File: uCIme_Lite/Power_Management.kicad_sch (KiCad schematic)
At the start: 13 parts

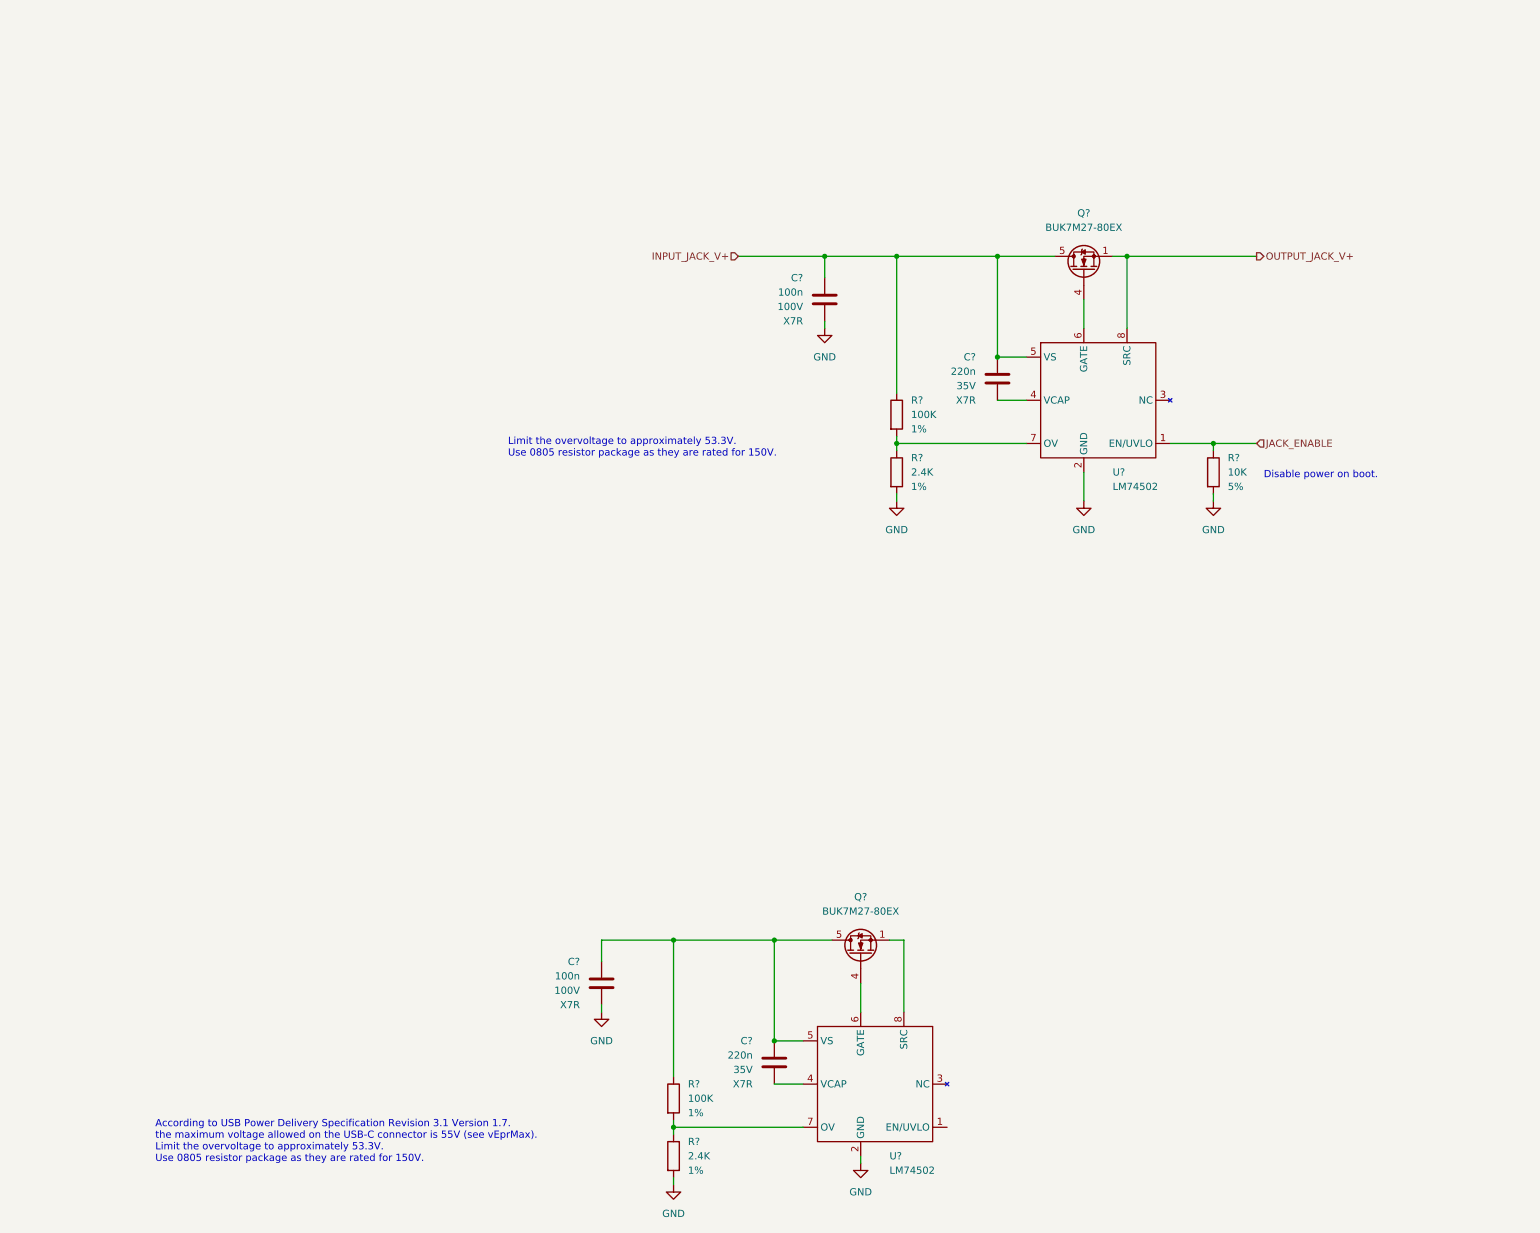
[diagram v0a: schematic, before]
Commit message: lite: Added USB-C connectors power control and data passthrough.
Signed-off-by: Adrien Ricciardi <aricciardi@baylibre.com>
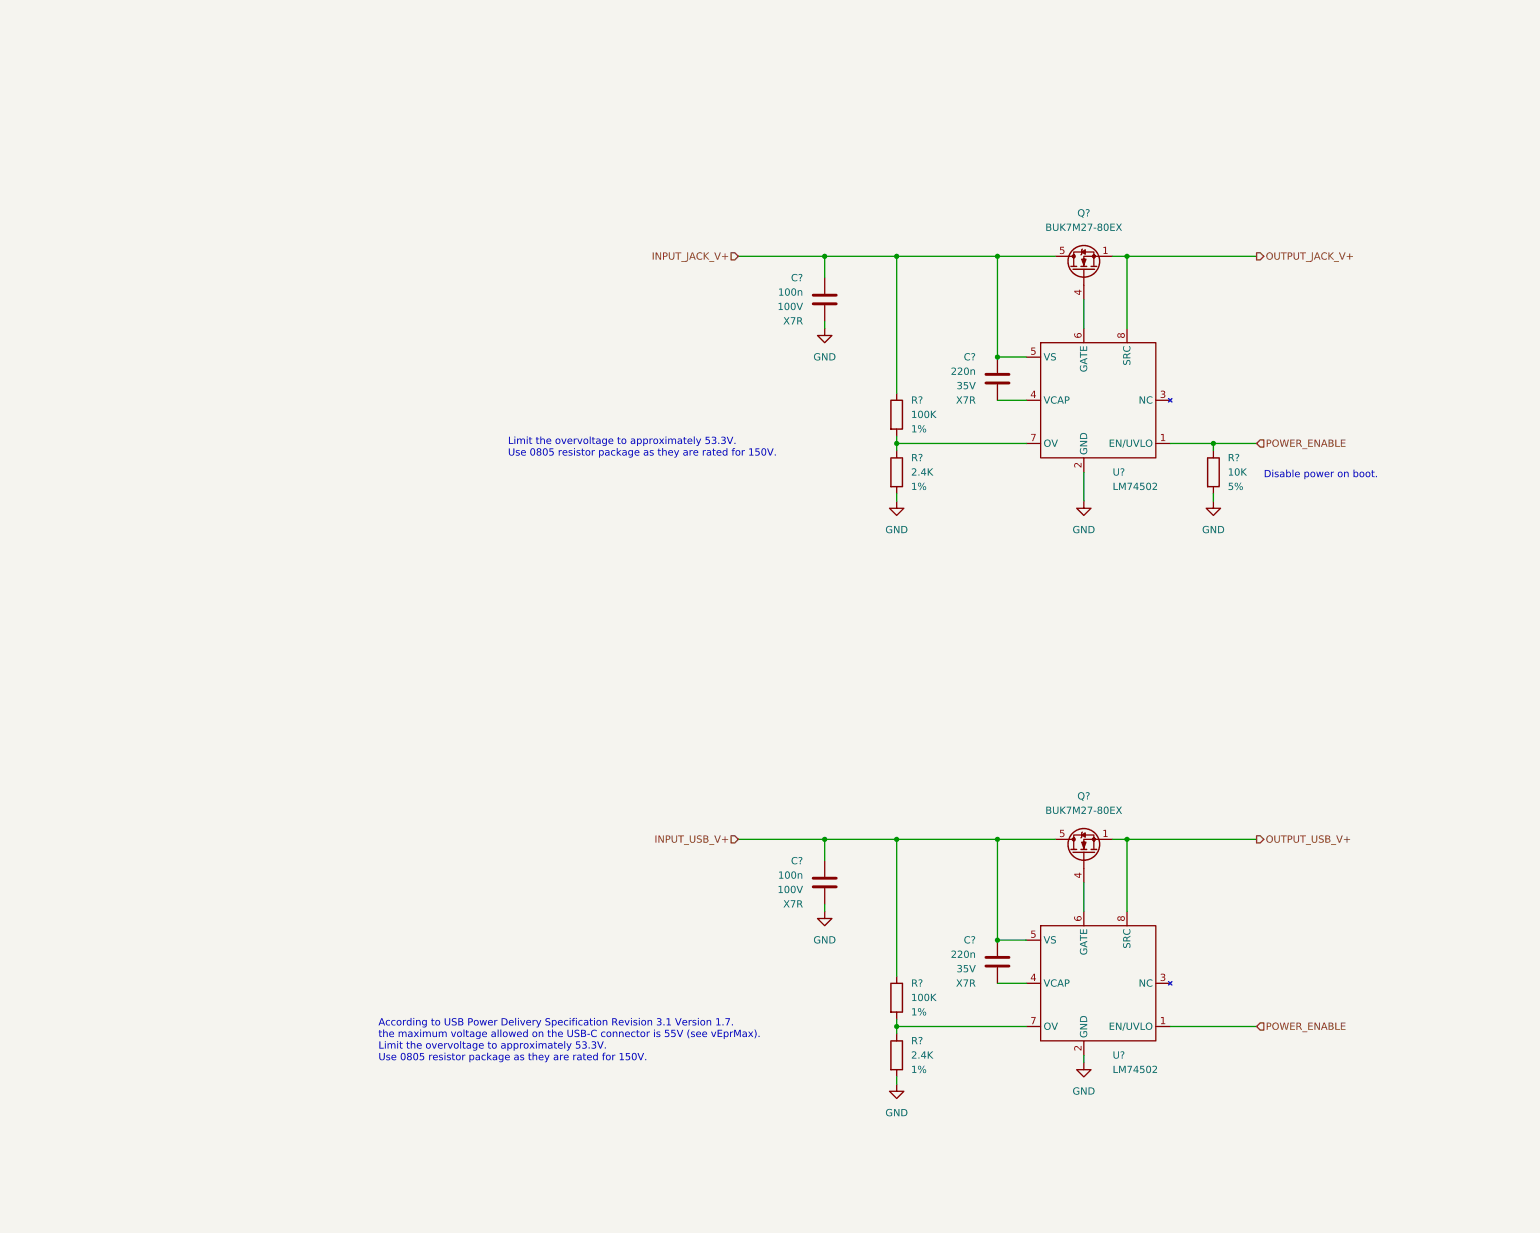
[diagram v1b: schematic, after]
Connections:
- net JACK_ENABLE is gone; now on net POWER_ENABLE: R?.1, U?.1 (EN/UVLO)
- net INPUT_USB_V+: now reaches C?.1, C?.1, Q?.5 (D), R?.1, U?.5 (VS)
- net OUTPUT_USB_V+: now reaches Q?.1 (S), Q?.2 (S), Q?.3 (S), U?.8 (SRC)
- net POWER_ENABLE: now reaches U?.1 (EN/UVLO)
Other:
- moved on the sheet: C?, Q?, R?, U?

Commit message: lite: Added FTDI USB connector, power supplies and USB differential pair to schematic.
Signed-off-by: Adrien Ricciardi <aricciardi@baylibre.com>
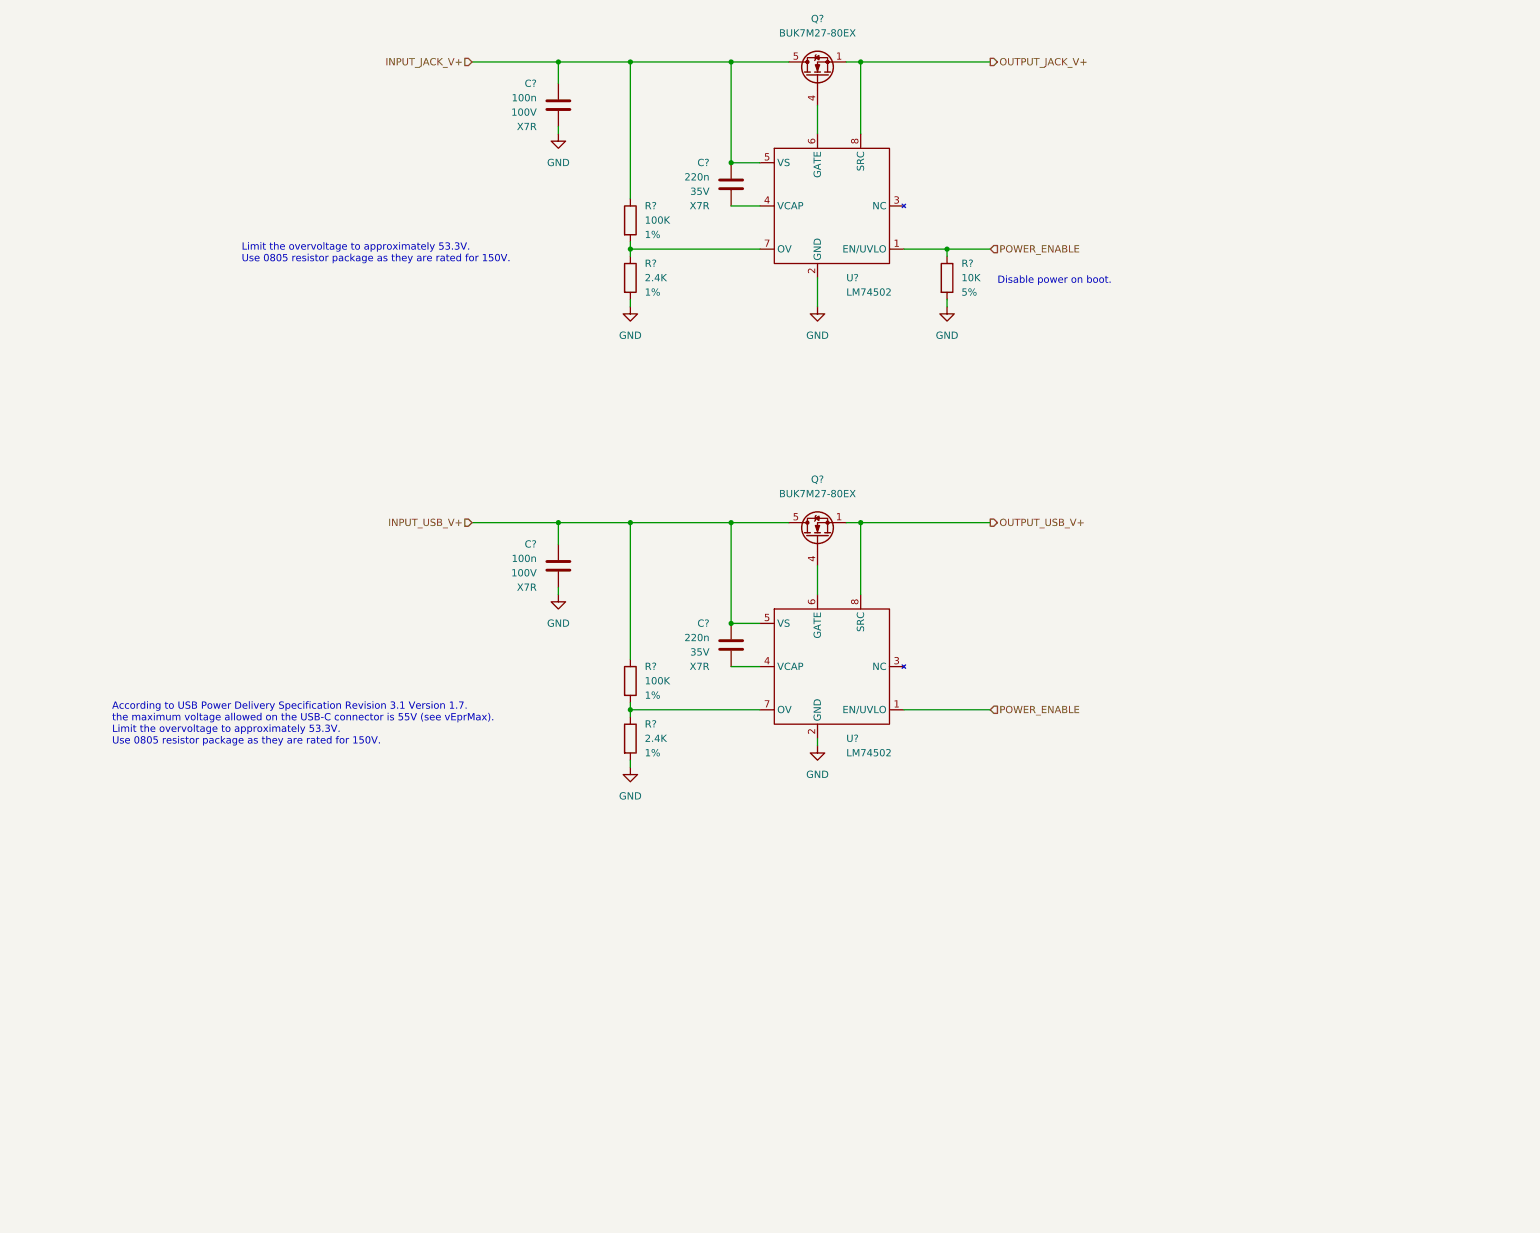
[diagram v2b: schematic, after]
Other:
- moved on the sheet: C?, Q?, R?, U?

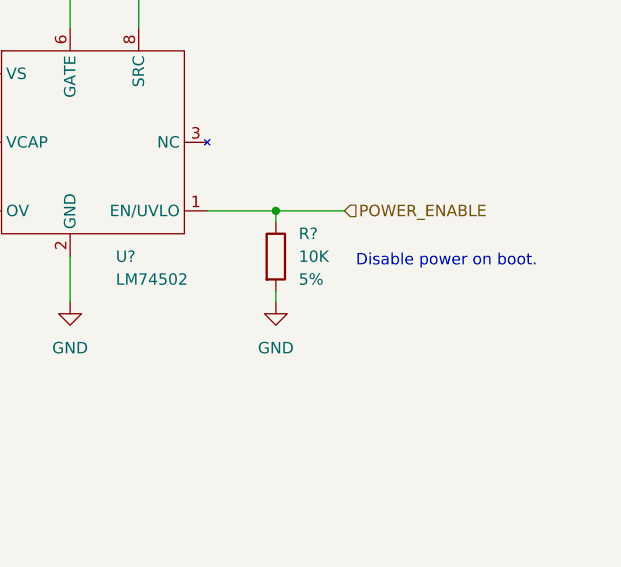
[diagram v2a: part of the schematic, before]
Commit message: lite: Added serial and USB connectors. A voltage translator is provided on the serial ports for the user to select the appropriate board voltage. No voltage translator is provided on the FTDI GPIO pins because they are meant to be used with custom extension boards.
Signed-off-by: Adrien Ricciardi <aricciardi@baylibre.com>
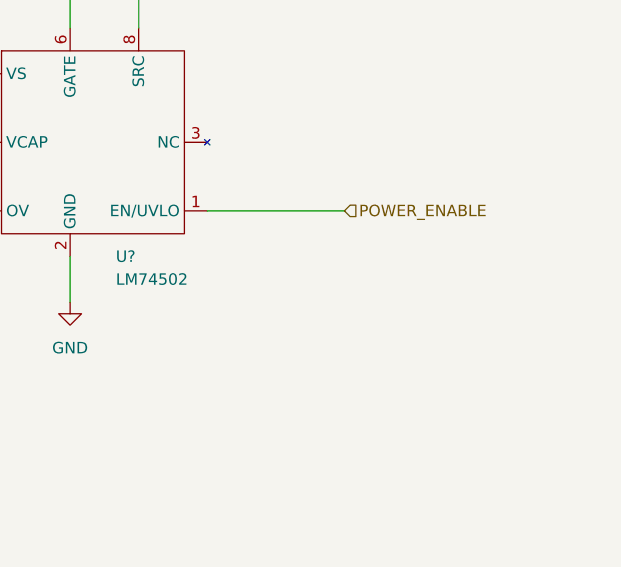
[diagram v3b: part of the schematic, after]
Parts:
- removed R?: 10K, Resistor_SMD:R_0603_1608Metric, symbol Device:R
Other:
- note removed: "Disable power on boot."
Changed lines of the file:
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@@
   (junction (at 132.08 59.69) (diameter 0) (color 0 0 0 0)
   )
-  (junction (at 187.96 59.69) (diameter 0) (color 0 0 0 0)
-  )
   (junction (at 119.38 26.67) (diameter 0) (color 0 0 0 0)
   )
@@
     (stroke (width 0) (type default) (color 0 0 0 0))
   )
-  (wire (pts (xy 187.96 59.69) (xy 195.58 59.69))
+  (wire (pts (xy 180.34 59.69) (xy 195.58 59.69))
     (stroke (width 0) (type default) (color 0 0 0 0))
   )
@@
     (stroke (width 0) (type default) (color 0 0 0 0))
   )
-  (wire (pts (xy 187.96 68.58) (xy 187.96 69.85))
-    (stroke (width 0) (type default) (color 0 0 0 0))
-  )
-  (wire (pts (xy 180.34 59.69) (xy 187.96 59.69))
-    (stroke (width 0) (type default) (color 0 0 0 0))
-  )
   (wire (pts (xy 149.86 107.95) (xy 149.86 125.73))
     (stroke (width 0) (type default) (color 0 0 0 0))
@@
   )
   (wire (pts (xy 119.38 26.67) (xy 119.38 30.48))
-    (stroke (width 0) (type default) (color 0 0 0 0))
-  )
-  (wire (pts (xy 187.96 59.69) (xy 187.96 60.96))
     (stroke (width 0) (type default) (color 0 0 0 0))
   )
@@
   (text "According to USB Power Delivery Specification Revision 3.1 Version 1.7.\nthe maximum voltage allowed on the USB-C connector is 55V (see vEprMax).\nLimit the overvoltage to approximately 53.3V.\nUse 0805 resistor package as they are rated for 150V."
     (at 40.64 147.32 0)
-    (effects (font (size 1.27 1.27)) (justify left bottom))
-  )
-  (text "Disable power on boot." (at 196.85 66.04 0)
     (effects (font (size 1.27 1.27)) (justify left bottom))
   )
@@
     (pin "8")
   )
-  (symbol (lib_id "Device:R") (at 187.96 64.77 0) (unit 1)
-    (in_bom yes) (on_board yes) (fields_autoplaced)
-    (property "Reference" "R?" (id 0) (at 190.5 62.2299 0)
-      (effects (font (size 1.27 1.27)) (justify left))
-    )
-    (property "Value" "10K" (id 1) (at 190.5 64.7699 0)
-      (effects (font (size 1.27 1.27)) (justify left))
-    )
-    (property "Footprint" "Resistor_SMD:R_0603_1608Metric" (id 2) (at 186.182 64.77 90)
-      (effects (font (size 1.27 1.27)) hide)
-    )
-    (property "Datasheet" "~" (id 3) (at 187.96 64.77 0)
-      (effects (font (size 1.27 1.27)) hide)
-    )
-    (property "PartNumber" "" (id 4) (at 187.96 64.77 0)
-      (effects (font (size 1.27 1.27)) hide)
-    )
-    (property "Value1" "5%" (id 5) (at 190.5 67.3099 0)
-      (effects (font (size 1.27 1.27)) (justify left))
-    )
-    (pin "1")
-    (pin "2")
-  )
   (symbol (lib_id "power:GND") (at 132.08 151.13 0) (unit 1)
     (in_bom yes) (on_board yes) (fields_autoplaced)
@@
     (pin "5")
   )
-  (symbol (lib_id "power:GND") (at 187.96 69.85 0) (unit 1)
-    (in_bom yes) (on_board yes) (fields_autoplaced)
-    (property "Reference" "#PWR?" (id 0) (at 187.96 76.2 0)
-      (effects (font (size 1.27 1.27)) hide)
-    )
-    (property "Value" "GND" (id 1) (at 187.96 74.93 0))
-    (property "Footprint" "" (id 2) (at 187.96 69.85 0)
-      (effects (font (size 1.27 1.27)) hide)
-    )
-    (property "Datasheet" "" (id 3) (at 187.96 69.85 0)
-      (effects (font (size 1.27 1.27)) hide)
-    )
-    (pin "1")
-  )
 )
